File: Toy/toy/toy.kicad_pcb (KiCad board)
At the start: 2 copper layers, 13 parts, among them J1 Conn_01x07_Pin, J2 Conn_01x03_Pin

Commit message: Routed PCB
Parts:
- added REF**: MountingHole_5.3mm_M5, MountingHole:MountingHole_5.3mm_M5, F.Cu at (202.5, 51.5)
- added REF**: MountingHole_5.3mm_M5, MountingHole:MountingHole_5.3mm_M5, F.Cu at (142.5, 151.5)
- added REF**: MountingHole_5.3mm_M5, MountingHole:MountingHole_5.3mm_M5, F.Cu at (262.5, 151.5)
- added REF**: MountingHole_5.3mm_M5, MountingHole:MountingHole_5.3mm_M5, F.Cu at (82.5, 151.5)
- added REF**: MountingHole_5.3mm_M5, MountingHole:MountingHole_5.3mm_M5, F.Cu at (202.5, 151.5)
- added REF**: MountingHole_5.3mm_M5, MountingHole:MountingHole_5.3mm_M5, F.Cu at (142.5, 51.5)
- added REF**: MountingHole_5.3mm_M5, MountingHole:MountingHole_5.3mm_M5, F.Cu at (82.5, 51.5)
- added REF**: MountingHole_5.3mm_M5, MountingHole:MountingHole_5.3mm_M5, F.Cu at (262.5, 51.5)
- A1, J1, R1, R2, R3, R4, R5, U5: moved to B.Cu
- moved U1 249.4 mm to (266.0, 93.0), turned to 180 degrees
- moved R1 191.8 mm to (249.0, 106.5), turned to 90 degrees
- moved U4 153.8 mm to (79.0, 109.0)
- moved U2 136.1 mm to (164.5, 42.5), turned to -90 degrees
- moved J1 132.5 mm to (188.2, 108.5), turned to 90 degrees
- moved R2 118.1 mm to (177.9, 59.0), turned to 180 degrees
- moved R4 108.5 mm to (101.0, 101.0), turned to 180 degrees
- moved A1 96.9 mm to (209.1, 88.1), turned to 90 degrees
- moved R5 73.5 mm to (155.5, 114.6), turned to 180 degrees
- moved J2 58.9 mm to (95.5, 138.4), turned to 180 degrees
- moved U5 45.8 mm to (153.0, 117.9), turned to 180 degrees
- moved U3 37.0 mm to (180.5, 159.5), turned to 90 degrees
- moved R3 14.7 mm to (177.4, 146.0), turned to 180 degrees
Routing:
- net GND: track 0.00 -> 359.9 mm
- net VDD: track 0.00 -> 357.3 mm
- net /C_sw4: track 0.00 -> 103.4 mm
- net /LED_ctrl: track 0.00 -> 100.3 mm
- net /C_sw1: track 0.00 -> 89.2 mm
- net /C_sw2: track 0.00 -> 73.1 mm
- net /C_sw3: track 0.00 -> 72.8 mm
- net /D1: track 53.5 -> 27.2 mm
- net /VT: track 53.5 -> 27.2 mm
- net /D0: track 53.5 -> 27.2 mm
- net /D3: track 53.5 -> 27.3 mm
- net /D2: track 53.5 -> 27.6 mm
- net Net-(U1-NO): track 0.00 -> 12.2 mm
- net Net-(U5-Vdd): track 25.5 -> 13.5 mm
- net Net-(U4-NO): track 0.00 -> 12.0 mm
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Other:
- board outline added: 190 x 120 mm

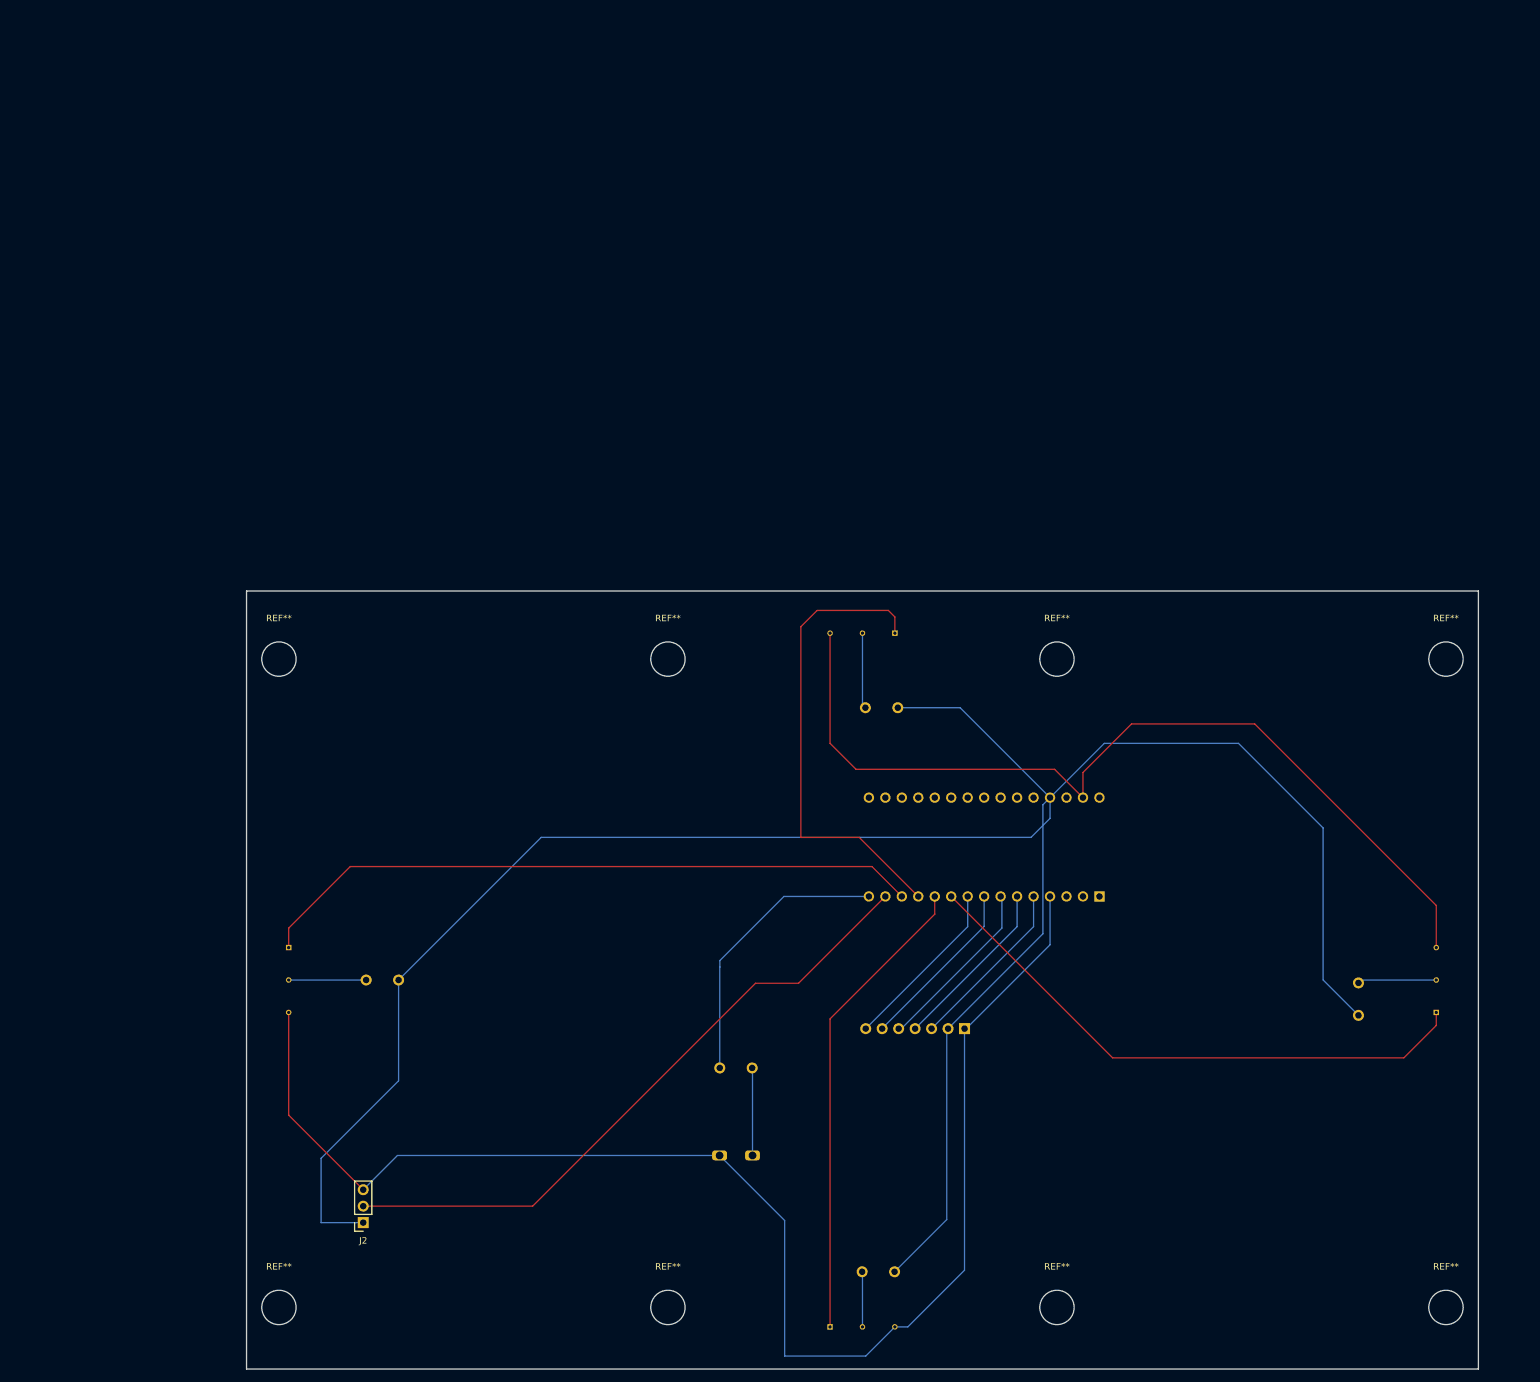
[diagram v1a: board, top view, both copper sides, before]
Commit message: V2
resistors changed
routing strategy
added more leds
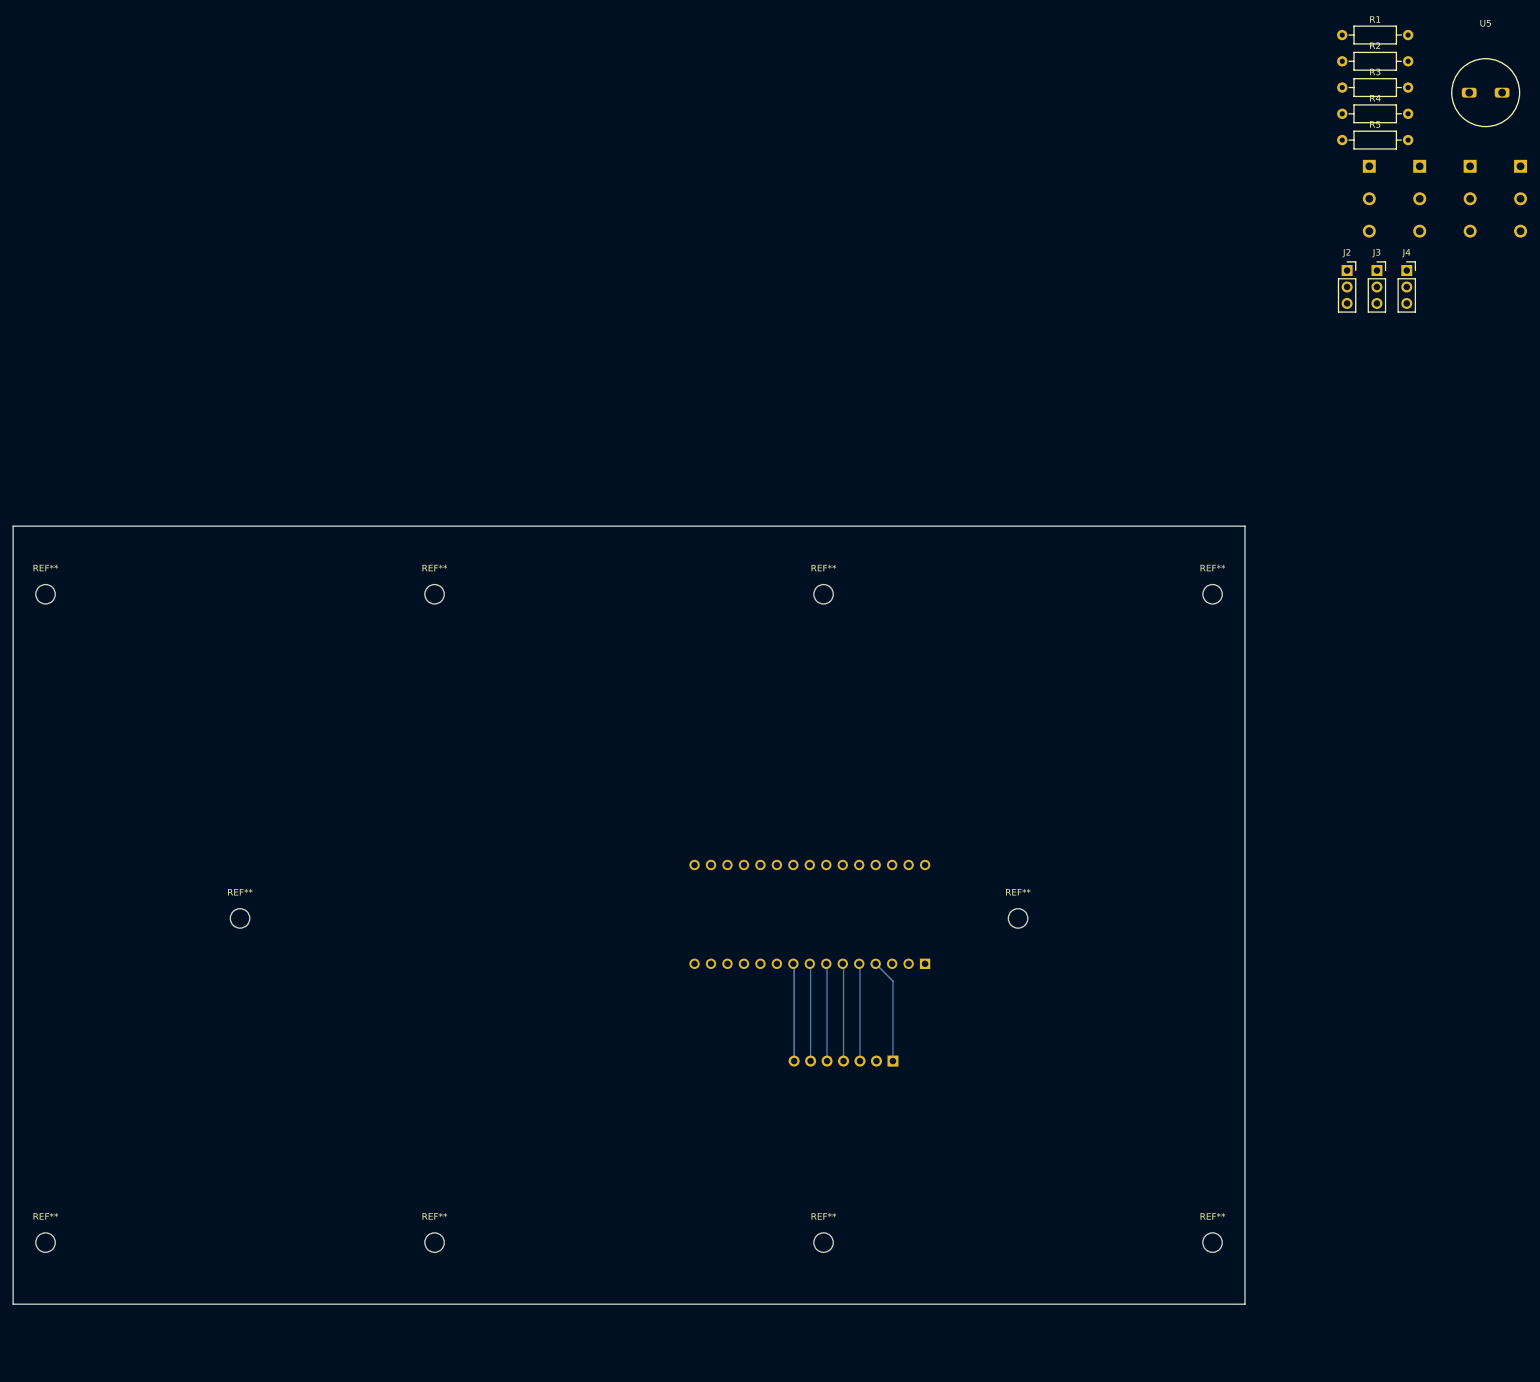
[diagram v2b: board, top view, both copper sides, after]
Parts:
- removed the REF** at (202.5, 51.5)
- removed the REF** at (142.5, 151.5)
- removed the REF** at (262.5, 151.5)
- removed the REF** at (82.5, 151.5)
- removed the REF** at (202.5, 151.5)
- removed the REF** at (142.5, 51.5)
- removed the REF** at (82.5, 51.5)
- removed the REF** at (262.5, 51.5)
- added J3: Conn_01x03_Pin, Connector_PinSocket_2.54mm:PinSocket_1x03_P2.54mm_Vertical, F.Cu at (251.8, -8.43)
- added J4: Conn_01x03_Pin, Connector_PinSocket_2.54mm:PinSocket_1x03_P2.54mm_Vertical, F.Cu at (256.4, -8.43)
- added REF**: MountingHole_3mm, MountingHole:MountingHole_3mm, F.Cu at (196.5, 91.5)
- added REF**: MountingHole_3mm, MountingHole:MountingHole_3mm, F.Cu at (106.5, 41.5)
- added REF**: MountingHole_3mm, MountingHole:MountingHole_3mm, F.Cu at (76.5, 91.5)
- added REF**: MountingHole_3mm, MountingHole:MountingHole_3mm, F.Cu at (166.5, 141.5)
- added REF**: MountingHole_3mm, MountingHole:MountingHole_3mm, F.Cu at (106.5, 141.5)
- added REF**: MountingHole_3mm, MountingHole:MountingHole_3mm, F.Cu at (226.5, 41.5)
- added REF**: MountingHole_3mm, MountingHole:MountingHole_3mm, F.Cu at (166.5, 41.5)
- added REF**: MountingHole_3mm, MountingHole:MountingHole_3mm, F.Cu at (46.5, 141.5)
- added REF**: MountingHole_3mm, MountingHole:MountingHole_3mm, F.Cu at (46.5, 41.5)
- added REF**: MountingHole_3mm, MountingHole:MountingHole_3mm, F.Cu at (226.5, 141.5)
- R1, R2, R3, R4, R5: footprint Crystal:Resonator-2Pin_W6.0mm_H3.0mm -> Resistor_THT:R_Axial_DIN0207_L6.3mm_D2.5mm_P10.16mm_Horizontal; moved to F.Cu
- U5: moved to F.Cu
- moved U4 225.0 mm to (269.0, -11.5)
- moved J2 211.2 mm to (247.2, -8.43), turned to 0 degrees
- moved U5 200.6 mm to (268.6, -46.0), turned to 0 degrees
- moved R4 197.6 mm to (246.5, -32.6), turned to 0 degrees
- moved R3 195.3 mm to (246.5, -36.6), turned to 0 degrees
- moved U3 189.1 mm to (261.2, -11.5), turned to 0 degrees
- moved R5 169.6 mm to (246.5, -28.6), turned to 0 degrees
- moved R1 151.2 mm to (246.5, -44.8), turned to 0 degrees
- moved R2 121.0 mm to (246.5, -40.7), turned to 0 degrees
- moved U1 106.5 mm to (245.7, -11.5), turned to 0 degrees
- moved U2 104.1 mm to (253.4, -11.5), turned to 0 degrees
- moved A1 28.8 mm to (182.2, 98.5)
- moved J1 12.1 mm to (177.2, 113.5)
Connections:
- net /LED_ctrl renamed /LED1_ctrl
- A1 pad 1: unconnected-(A1-TX1-Pad1) -> /BUZZ
- A1 pad 15: /BUZZ -> /LED2_ctrl
- A1 pad 16: unconnected-(A1-SCK-Pad16) -> /LED3_ctrl
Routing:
- net VDD: track 357.3 -> 0.00 mm
- net GND: track 359.9 -> 16.1 mm
- net /C_sw4: track 103.4 -> 0.00 mm
- net /LED1_ctrl: track 100.3 -> 0.00 mm
- net /C_sw1: track 89.2 -> 0.00 mm
- net /C_sw2: track 73.1 -> 0.00 mm
- net /C_sw3: track 72.8 -> 0.00 mm
- net /BUZZ: track 43.7 -> 0.00 mm
- net Net-(U5-Vdd): track 13.5 -> 0.00 mm
- net /D2: track 27.6 -> 15.0 mm
- net /D3: track 27.3 -> 15.0 mm
- net Net-(U1-NO): track 12.2 -> 0.00 mm
- net /VT: track 27.2 -> 15.0 mm
- net /D0: track 27.2 -> 15.0 mm
- net /D1: track 27.2 -> 15.0 mm
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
